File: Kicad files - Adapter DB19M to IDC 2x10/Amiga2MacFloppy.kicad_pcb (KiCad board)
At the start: 2 copper layers, 30 x 40 mm, 4 parts, among them J2 Conn_02x10_Odd_Even_MountingP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, J5 DB19M

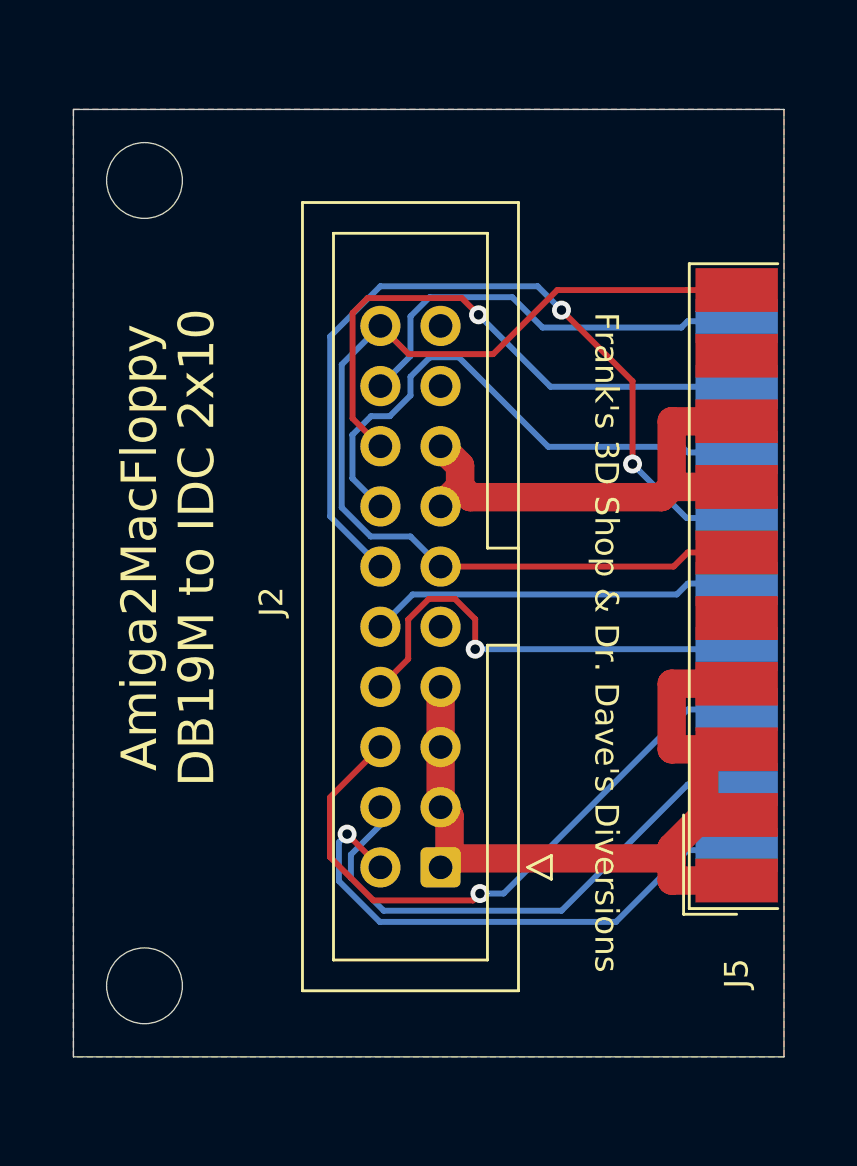
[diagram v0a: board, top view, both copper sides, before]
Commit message: Corrections
Corrected Adapter to Female connector instead of male.
Removed R1
Cleaned up schematics
Added Open Hardware Logo
Cleaned up silkscreens
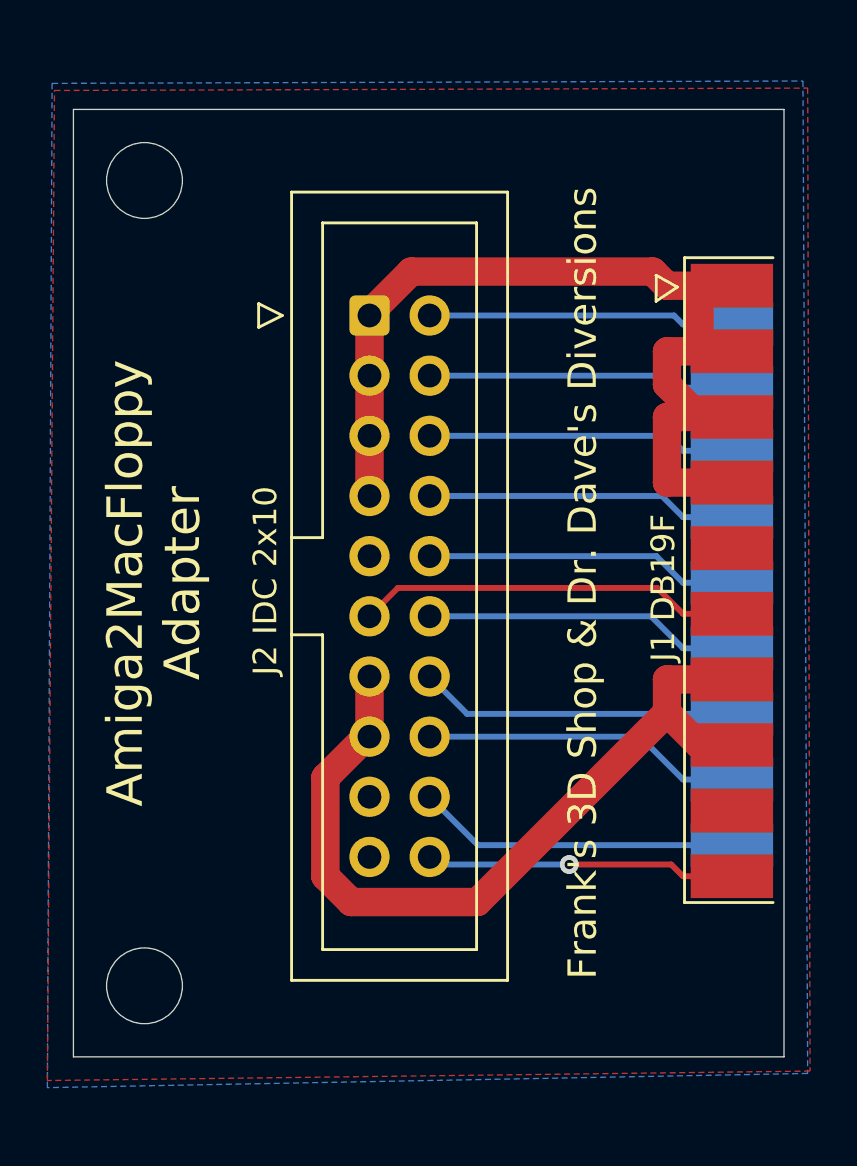
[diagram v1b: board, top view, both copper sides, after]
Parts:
- removed J5: DB19M, Amiga2MacFloppy:DSUB-19_Male_EdgeMount_P2.77mm
- added J1 DB19F: DB19F, Amiga2MacFloppy:DSUB-19_Female_EdgeMount_P2.77mm, F.Cu at (158.3, 108.2)
- added Open Harware Logo BAck: OSHW-Logo2_9.8x8mm_SilkScreen, Symbol:OSHW-Logo2_9.8x8mm_SilkScreen, B.Cu at (136.2, 108.5)
- J2 IDC 2x10: renamed from J2
- moved J2 IDC 2x10 23.5 mm to (143.0, 96.9), turned to 0 degrees
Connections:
- J2 IDC 2x10 pad 11: PWM -> +5V
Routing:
- net PWM: track 42.9 -> 13.1 mm, vias 0 -> 1
- net SEL: track 34.7 -> 13.3 mm, vias 2 -> 0
- net +5V: track 0.00 -> 16.2 mm
- net +12V: track 20.8 -> 34.9 mm
- net PH2: track 26.8 -> 13.0 mm, vias 1 -> 0
- net RD: track 24.1 -> 13.5 mm, vias 1 -> 0
- net PH0: track 22.9 -> 12.9 mm, vias 1 -> 0
- net _ENABLE: track 23.2 -> 13.4 mm
- net DIR: track 22.6 -> 13.0 mm
- net PH3: track 19.2 -> 13.1 mm, vias 1 -> 0
- net GND: track 35.8 -> 41.1 mm
- net WR: track 18.2 -> 13.6 mm
- net _DKWE: track 15.8 -> 13.2 mm
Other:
- board text added: "Amiga2MacFloppy Adapter"
- board text removed: "Amiga2MacFloppy DB19M to IDC 2x10"
